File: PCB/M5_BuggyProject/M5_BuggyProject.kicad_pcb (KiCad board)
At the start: 2 copper layers, 40.6 x 94 mm, 27 parts, among them J1 XT60, J2 VCC, J3 10V, J4 RF Receiver

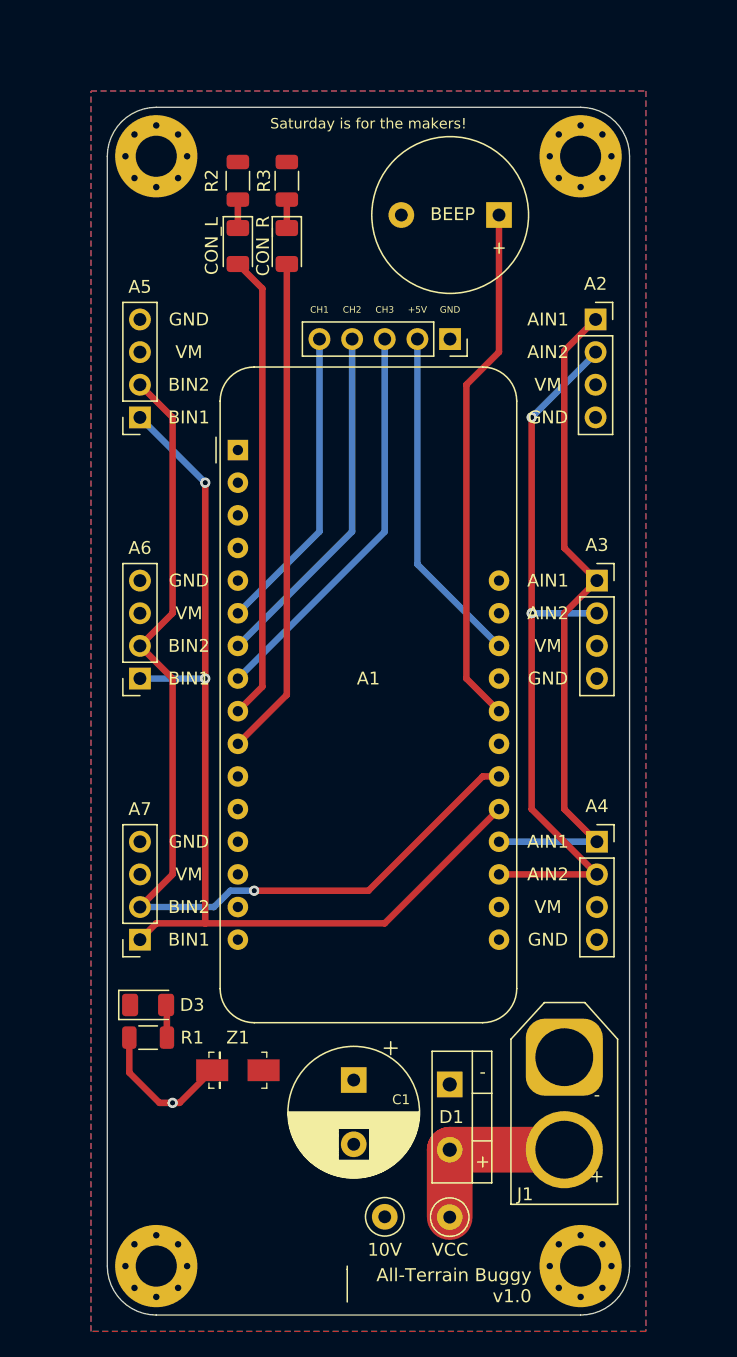
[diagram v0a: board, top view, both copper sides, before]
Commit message: Increased board size for trace width.
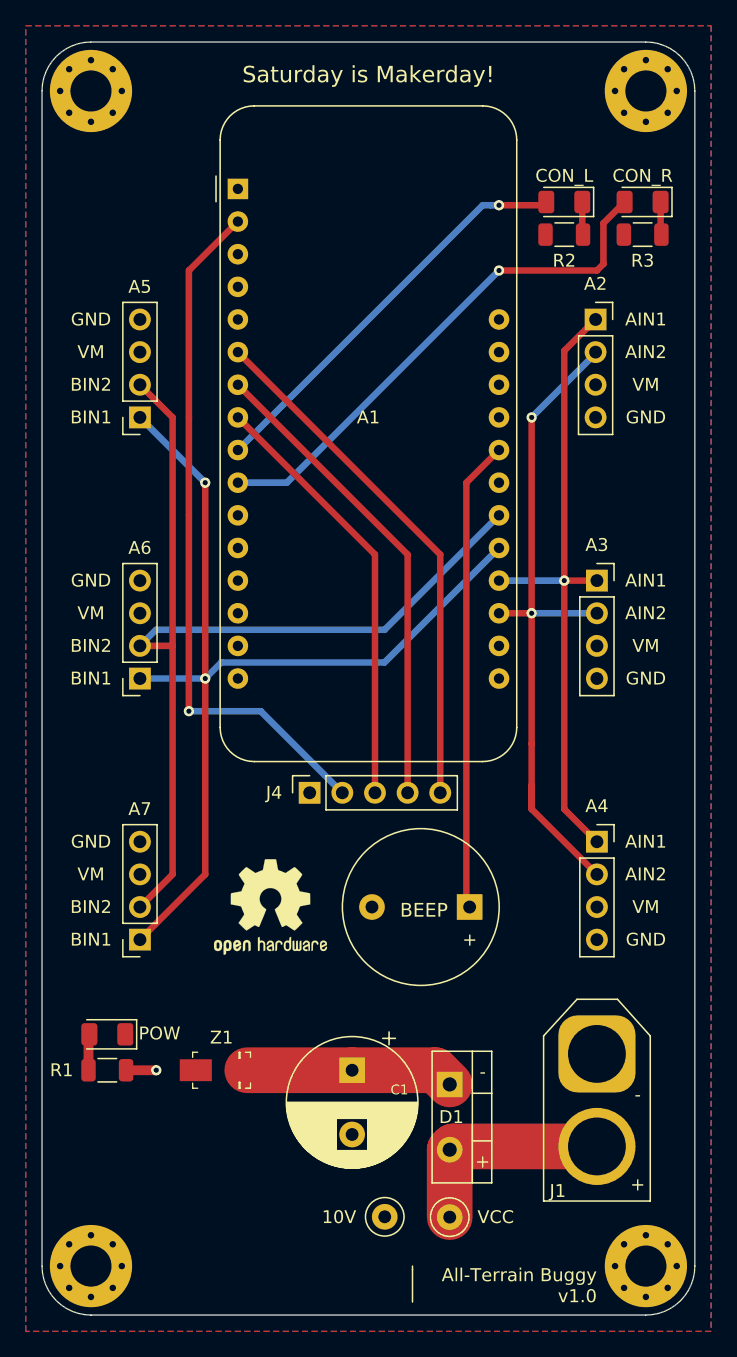
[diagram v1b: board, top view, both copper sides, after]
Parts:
- added REF**: OSHW-Logo2_9.8x8mm_SilkScreen, Symbol:OSHW-Logo2_9.8x8mm_SilkScreen, F.Cu at (89.4, 93.7)
- J4: value RF Receiver -> Receiver
- moved BZ1 53.9 mm to (104.9, 93.7)
- moved J4 37.0 mm to (92.5, 84.8), turned to 90 degrees
- moved R3 28.0 mm to (118.4, 41.4), turned to 180 degrees
- moved D4 27.9 mm to (118.4, 38.9), turned to 180 degrees
- moved R2 25.7 mm to (112.3, 41.4), turned to 180 degrees
- moved D2 25.6 mm to (112.3, 38.9), turned to 180 degrees
- moved A1 20.3 mm to (86.9, 37.8)
- moved H1 7.18 mm to (75.4, 30.2)
- moved H2 7.18 mm to (118.6, 30.2)
- moved G*** 5.52 mm to (73.9, 111.1)
- moved H3 5.08 mm to (118.6, 121.7)
- moved H4 5.08 mm to (75.4, 121.7)
- moved R1 4.07 mm to (76.7, 106.4), turned to 0 degrees
- moved D3 3.91 mm to (76.7, 103.6), turned to 180 degrees
- moved G*** 3.14 mm to (86.4, 118.9)
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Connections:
- J4 pad 2: +5V -> +3V3
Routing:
- net +3V3: track 0.00 -> 54.5 mm, vias 0 -> 1
- net +5V: track 26.5 -> 0.00 mm
- net CHANNEL_1: track 24.0 -> 40.8 mm
- net CHANNEL_2: track 27.6 -> 37.2 mm
- net +10V: track 11.2 -> 18.6 mm
- net CONFIG_L: track 36.4 -> 32.0 mm, vias 0 -> 1
- net BEEP: track 40.7 -> 36.7 mm
- net AIN2: track 57.5 -> 54.3 mm
- net VCC: track 14.2 -> 16.8 mm
- net CHANNEL_3: track 31.2 -> 33.6 mm
- net AIN1: track 52.4 -> 50.3 mm, vias 0 -> 1
- net CONFIG_R: track 38.9 -> 41.0 mm, vias 0 -> 1
- net BIN1: track 78.7 -> 77.0 mm
- net BIN2: track 77.0 -> 77.4 mm, vias 1 -> 0
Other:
- board size 40.6 x 94 mm -> 50.8 x 99.1 mm
- board text added: "POW"
- board text added: "Saturday is Makerday!"
- board text removed: "+5V"
- board text removed: "CH1"
- board text removed: "CH2"
- board text removed: "CH3"
- board text removed: "Saturday is for the makers!"

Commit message: Moved config LEDs, added OSH logo.
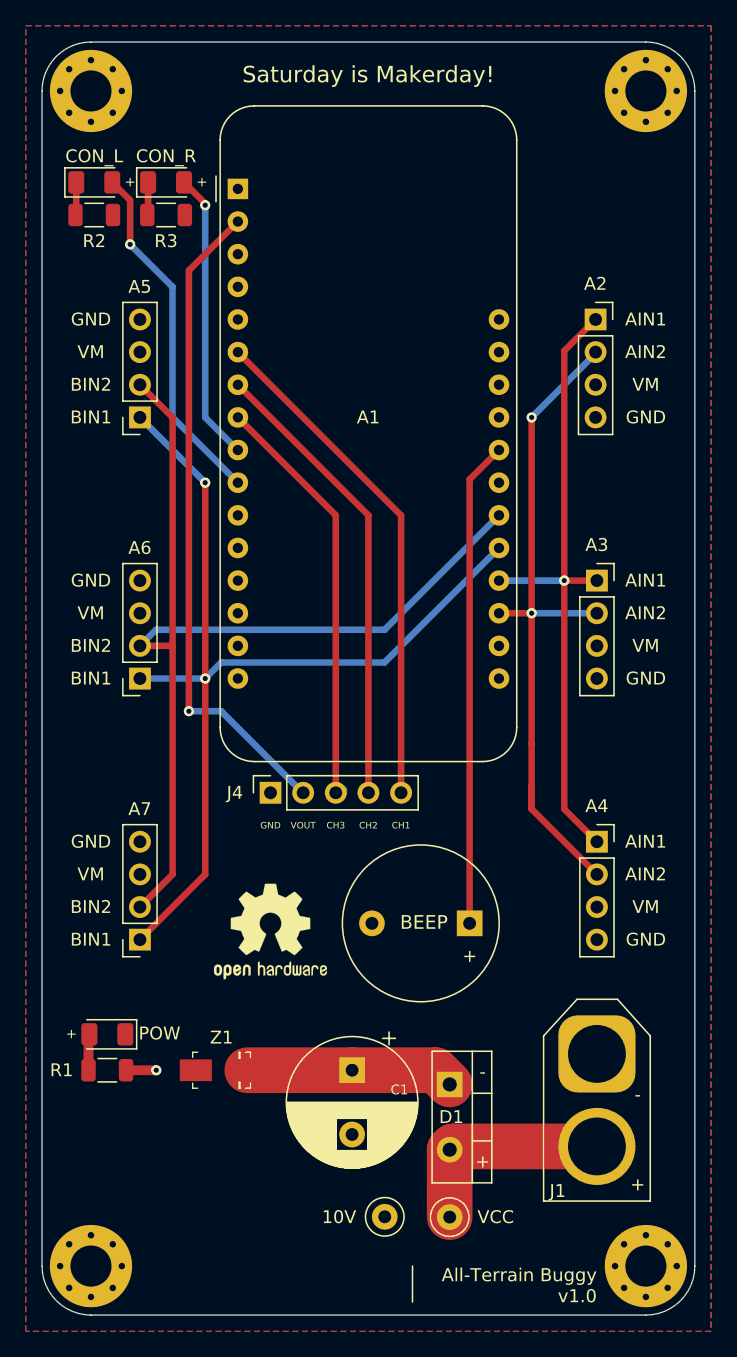
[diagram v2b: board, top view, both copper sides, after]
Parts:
- moved D4 37.1 mm to (81.3, 37.3), turned to 0 degrees
- moved R3 37.1 mm to (81.3, 39.9), turned to 0 degrees
- moved D2 36.6 mm to (75.7, 37.3), turned to 0 degrees
- moved R2 36.6 mm to (75.7, 39.9), turned to 0 degrees
- moved J4 3.05 mm to (89.4, 84.8)
- moved REF** 1.91 mm to (89.4, 95.6)
- moved BZ1 1.27 mm to (104.9, 95.0)
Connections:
- A1 pad 10: CONFIG_R -> CONFIG_L
- A1 pad 9: CONFIG_L -> CONFIG_R
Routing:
- net CONFIG_R: track 41.0 -> 22.6 mm
- net CONFIG_L: track 32.0 -> 27.4 mm
- net +3V3: track 54.5 -> 51.2 mm
- net CHANNEL_1: track 40.8 -> 39.6 mm
- net CHANNEL_2: track 37.2 -> 36.0 mm
- net BEEP: track 36.7 -> 37.8 mm
- net CHANNEL_3: track 33.6 -> 32.6 mm
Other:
- board text added: "CH1"
- board text added: "CH2"
- board text added: "CH3"
- board text added: "VOUT"
